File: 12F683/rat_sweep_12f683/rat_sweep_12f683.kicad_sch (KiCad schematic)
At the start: 13 parts, among them J1 Conn_01x01_Pin, J2 Conn_01x01_Pin, P1 USB_C_Plug_USB2.0, U1 PIC12F683-xP, U2 TLC272, U3 AMS1117-3.3

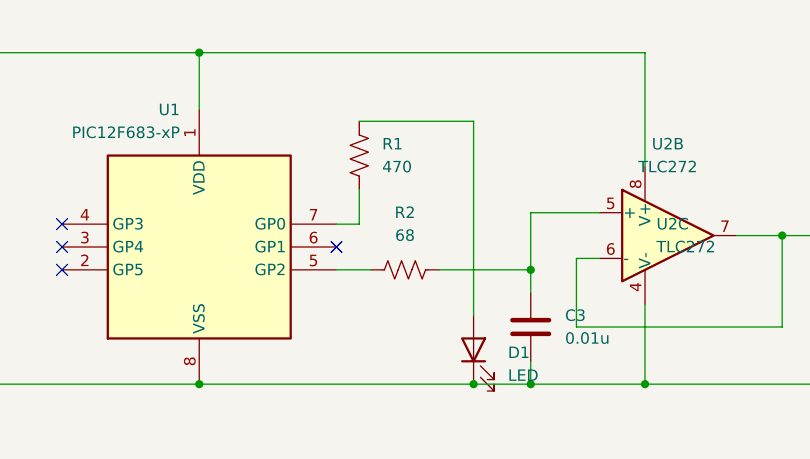
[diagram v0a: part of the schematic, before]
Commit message: Change R2 to 470.
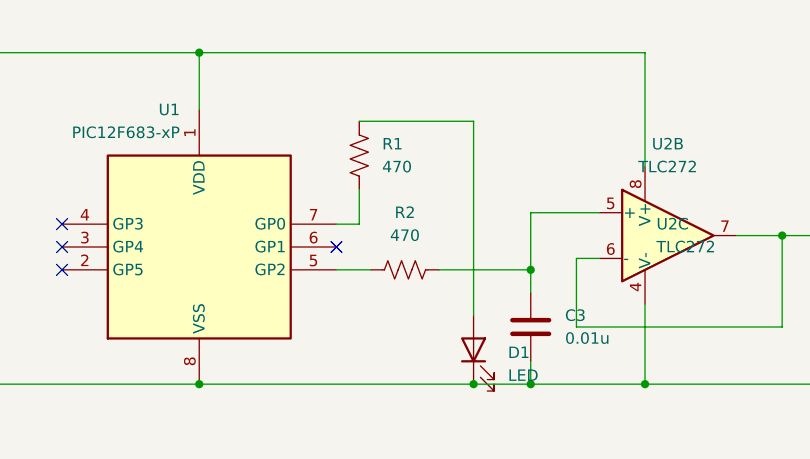
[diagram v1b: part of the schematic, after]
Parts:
- R2: value 68 -> 470
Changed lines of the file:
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@@
 			)
 		)
-		(property "Value" "68"
+		(property "Value" "470"
 			(at 177.8 99.06 90)
 			(effects
